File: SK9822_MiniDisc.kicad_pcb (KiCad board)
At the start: 4 copper layers, 220 x 220 mm, 381 parts, among them P1 CONN_01X04, P2 CONN_01X04

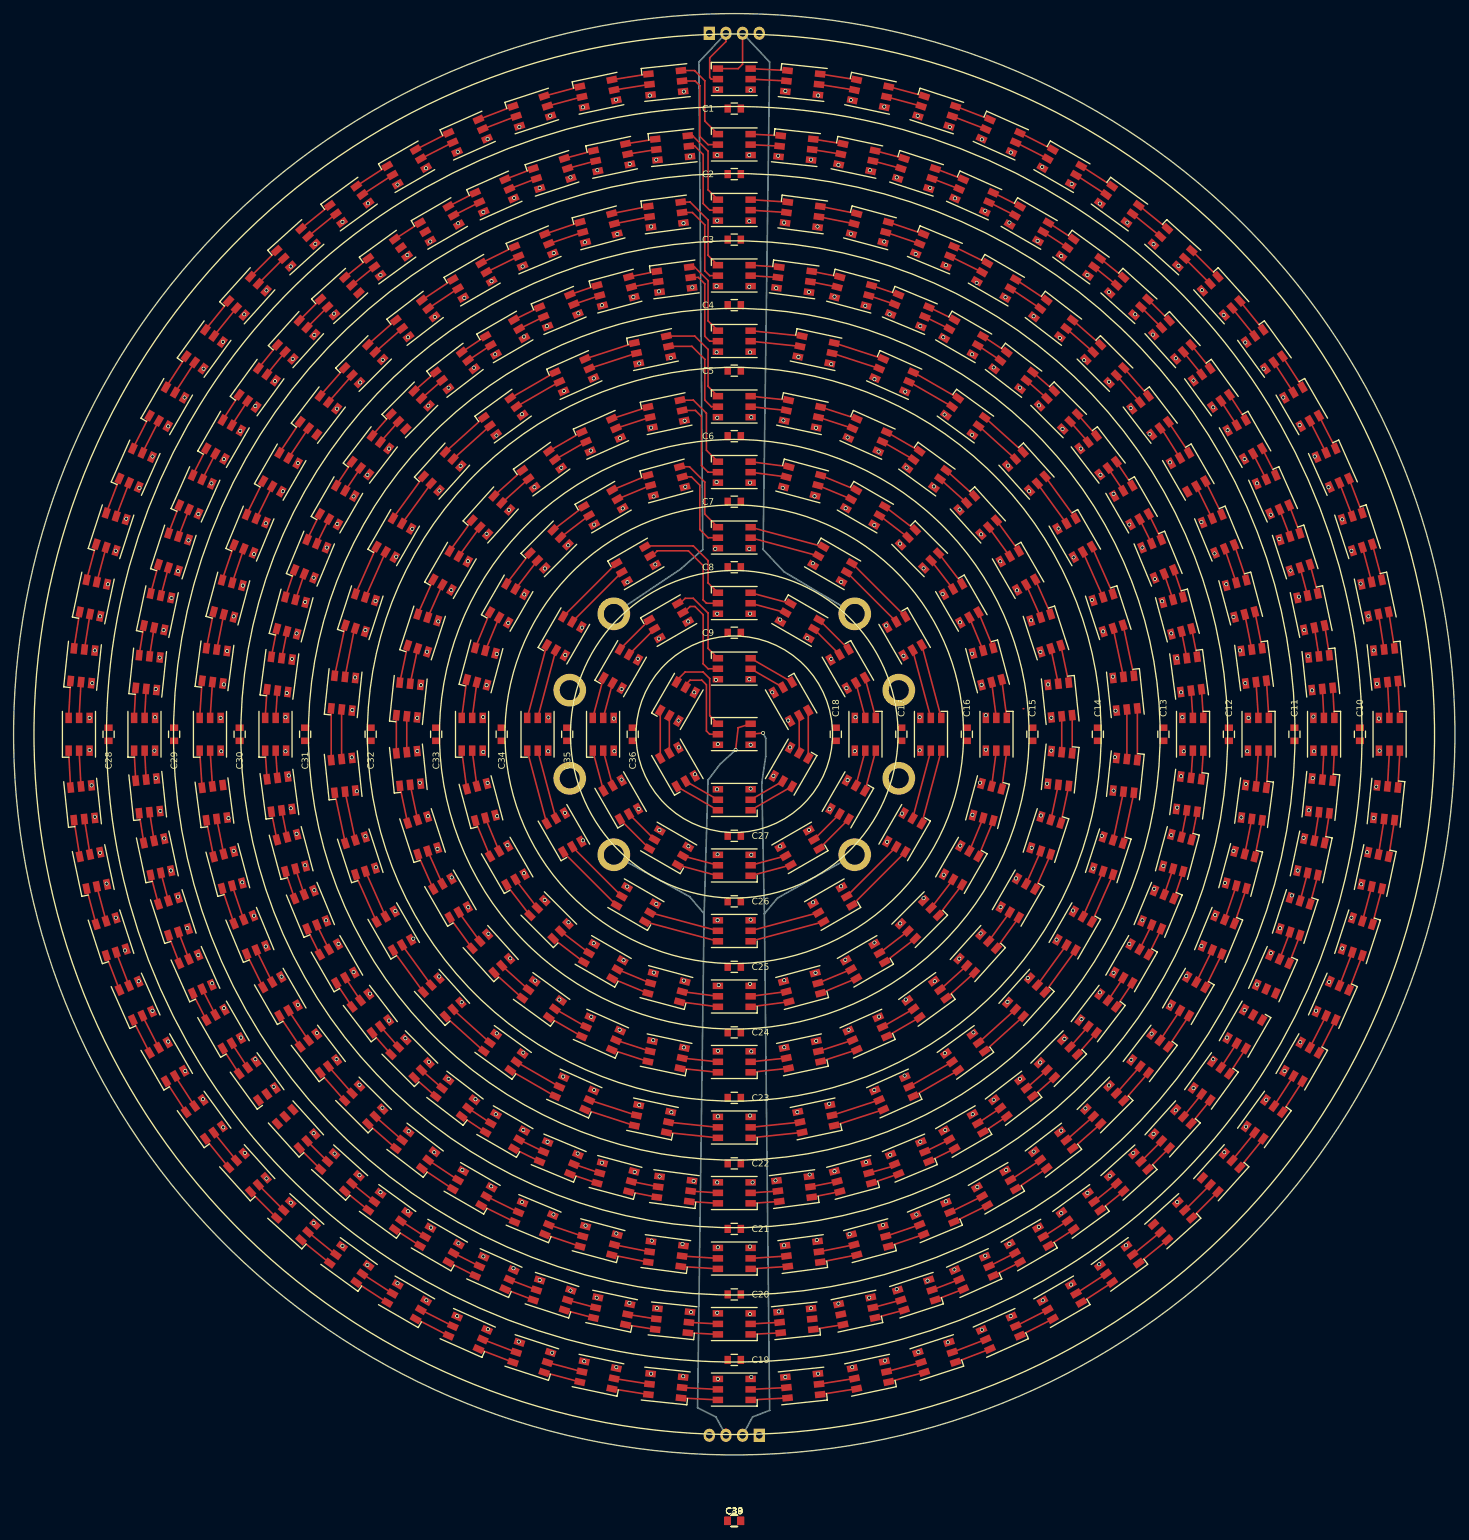
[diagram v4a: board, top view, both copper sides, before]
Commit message: everything routed
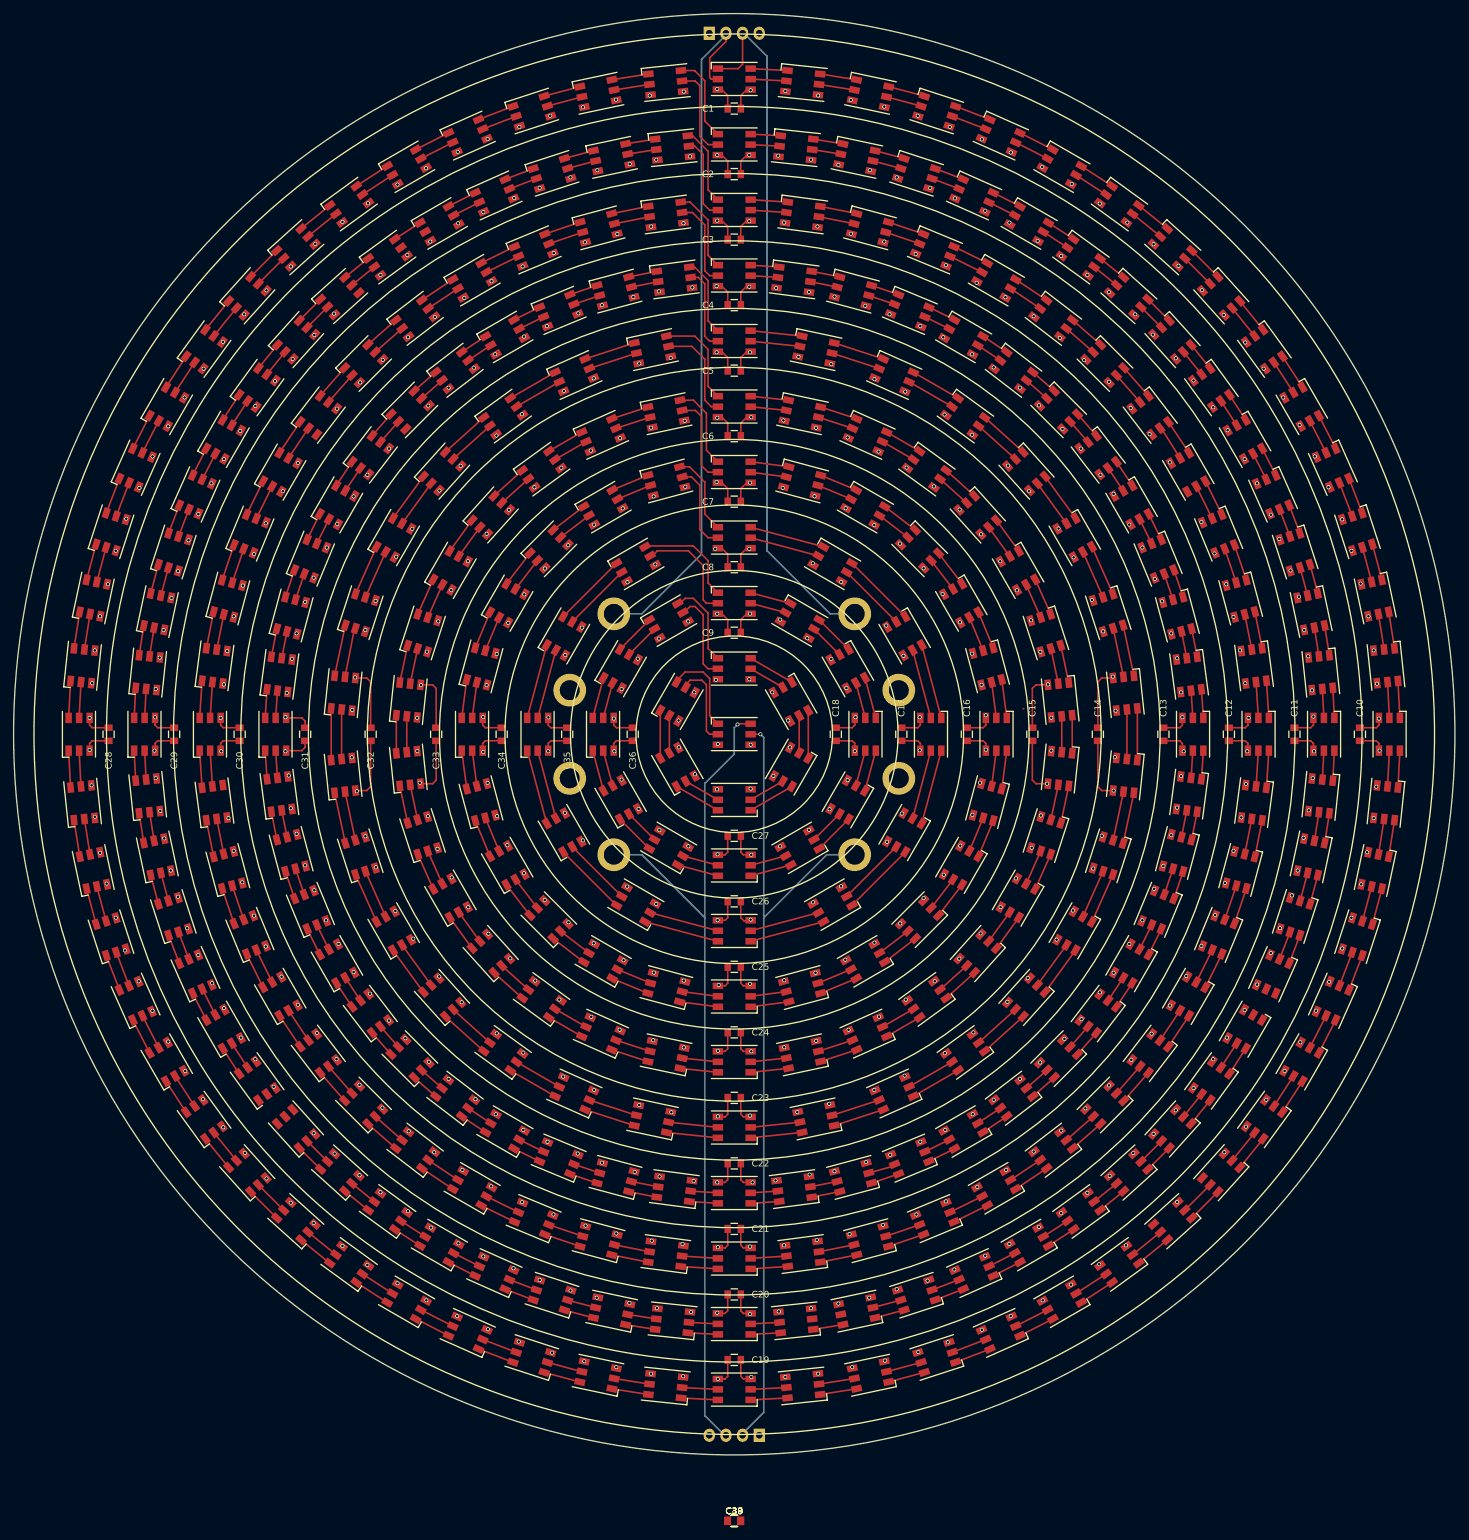
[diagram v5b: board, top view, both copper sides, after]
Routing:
- net GND: track 4051.5 -> 4218.6 mm
- net VCC: track 4018.1 -> 4185.0 mm
- net Net-(D331-Pad6): track 132.2 -> 133.7 mm
- net Net-(D1-Pad2): track 106.4 -> 107.3 mm

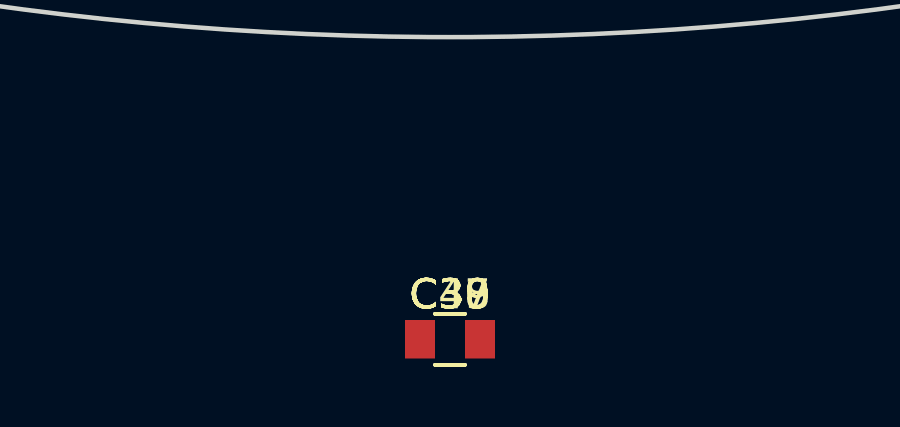
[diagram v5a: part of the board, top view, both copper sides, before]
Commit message: removed extraneous caps
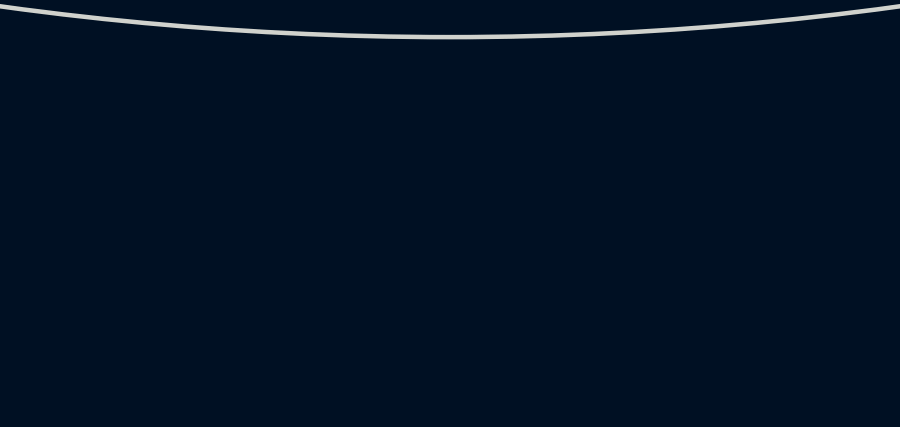
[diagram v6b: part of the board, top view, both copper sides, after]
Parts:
- removed C37, C38, C39, C40: 10uF, Capacitors_SMD:C_0805

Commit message: added copper pours
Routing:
- added copper zone on Gnd.Cu, net GND
- added copper zone on Pwr.Cu, net VCC
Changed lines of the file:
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@@
   (general
     (links 1408)
-    (no_connects 16)
-    (area 189.924999 87.966666 410.075001 322.900001)
+    (no_connects 14)
+    (area 189.924999 87.966666 410.075001 312.033333)
     (thickness 1.6)
     (drawings 11)
@@
   (page A2)
   (layers
-    (0 F.Cu signal)
-    (1 Gnd.Cu power)
-    (2 Pwr.Cu power)
-    (31 B.Cu signal)
+    (0 F.Cu signal hide)
+    (1 Gnd.Cu power hide)
+    (2 Pwr.Cu power hide)
+    (31 B.Cu signal hide)
     (32 B.Adhes user)
     (33 F.Adhes user)
@@
   (segment (start 299.25 306.48) (end 298.73 307) (width 0.25) (layer B.Cu) (net 666))
   (segment (start 298.73 307) (end 298.75 307) (width 0.25) (layer B.Cu) (net 666))
+  (zone (net 4) (net_name GND) (layer Gnd.Cu) (hatch edge 0.508)
+    (connect_pads (clearance 0.508))
+    (min_thickness 0.254)
+    (fill yes (arc_segments 16) (thermal_gap 0.508) (thermal_bridge_width 0.508) (smoothing fillet))
+    (polygon
+      (pts
+        (xy 191 200) (xy 191 187) (xy 192 181) (xy 193 176) (xy 194 172)
+        (xy 195 168) (xy 196 165) (xy 197 162) (xy 199 157) (xy 200 155)
+        (xy 201 153) (xy 203 149) (xy 205 145) (xy 208 140) (xy 210 137)
+        (xy 213 133) (xy 217 128) (xy 227 118) (xy 233 113) (xy 240 108)
+        (xy 245 105) (xy 257 99) (xy 262 97) (xy 265 96) (xy 268 95)
+        (xy 272 94) (xy 276 93) (xy 280 92) (xy 287 91) (xy 298 91)
+        (xy 313 91) (xy 320 92) (xy 325 93) (xy 329 94) (xy 338 97)
+        (xy 343 99) (xy 355 105) (xy 360 108) (xy 363 110) (xy 367 113)
+        (xy 373 118) (xy 382 127) (xy 383 128) (xy 387 133) (xy 390 137)
+        (xy 392 140) (xy 395 145) (xy 401 157) (xy 403 162) (xy 406 171)
+        (xy 408 180) (xy 409 186) (xy 409 213) (xy 408 220) (xy 407 225)
+        (xy 405 232) (xy 403 238) (xy 401 243) (xy 395 255) (xy 392 260)
+        (xy 387 267) (xy 383 272) (xy 373 282) (xy 367 287) (xy 363 290)
+        (xy 360 292) (xy 355 295) (xy 343 301) (xy 338 303) (xy 332 305)
+        (xy 325 307) (xy 320 308) (xy 314 309) (xy 286 309) (xy 280 308)
+        (xy 275 307) (xy 271 306) (xy 262 303) (xy 257 301) (xy 245 295)
+        (xy 237 290) (xy 233 287) (xy 228 283) (xy 217 272) (xy 213 267)
+        (xy 208 260) (xy 205 255) (xy 199 243) (xy 197 238) (xy 196 235)
+        (xy 195 232) (xy 194 229) (xy 193 225) (xy 192 220) (xy 191 214)
+      )
+    )
+  )
+  (zone (net 1) (net_name VCC) (layer Pwr.Cu) (hatch edge 0.508)
+    (connect_pads (clearance 0.508))
+    (min_thickness 0.254)
+    (fill yes (arc_segments 16) (thermal_gap 0.508) (thermal_bridge_width 0.508))
+    (polygon
+      (pts
+        (xy 320 92) (xy 325 93) (xy 329 94) (xy 338 97) (xy 343 99)
+        (xy 355 105) (xy 360 108) (xy 363 110) (xy 367 113) (xy 373 118)
+        (xy 383 128) (xy 387 133) (xy 390 137) (xy 392 140) (xy 395 145)
+        (xy 401 157) (xy 403 162) (xy 406 171) (xy 408 180) (xy 409 186)
+        (xy 409 213) (xy 408 220) (xy 407 225) (xy 405 232) (xy 403 238)
+        (xy 401 243) (xy 395 255) (xy 392 260) (xy 387 267) (xy 383 272)
+        (xy 373 282) (xy 367 287) (xy 363 290) (xy 360 292) (xy 355 295)
+        (xy 343 301) (xy 338 303) (xy 332 305) (xy 325 307) (xy 320 308)
+        (xy 314 309) (xy 286 309) (xy 280 308) (xy 275 307) (xy 271 306)
+        (xy 262 303) (xy 257 301) (xy 245 295) (xy 237 290) (xy 228 283)
+        (xy 217 272) (xy 213 267) (xy 208 260) (xy 205 255) (xy 199 243)
+        (xy 197 238) (xy 194 229) (xy 193 225) (xy 192 220) (xy 191 214)
+        (xy 191 187) (xy 192 181) (xy 193 176) (xy 195 168) (xy 197 162)
+        (xy 199 157) (xy 205 145) (xy 208 140) (xy 210 137) (xy 213 133)
+        (xy 217 128) (xy 227 118) (xy 233 113) (xy 240 108) (xy 245 105)
+        (xy 257 99) (xy 262 97) (xy 268 95) (xy 280 92) (xy 287 91)
+        (xy 313 91)
+      )
+    )
+  )
 )

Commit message: added lables
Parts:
- P1, P2: footprint Conn:Angled_1x4 -> Conn:Angled_nosilk_1x4
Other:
- board text added: "5V"
- board text added: "CLK"
- board text added: "DAT"
- board text added: "GND"
